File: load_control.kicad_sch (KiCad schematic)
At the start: 17 parts, among them Q20 BSB280N15NZ3, Q21 Q_NMOS_DGS, Q22 Q_NMOS_DGS, Q23 Q_NMOS_DGS, U20 LM358

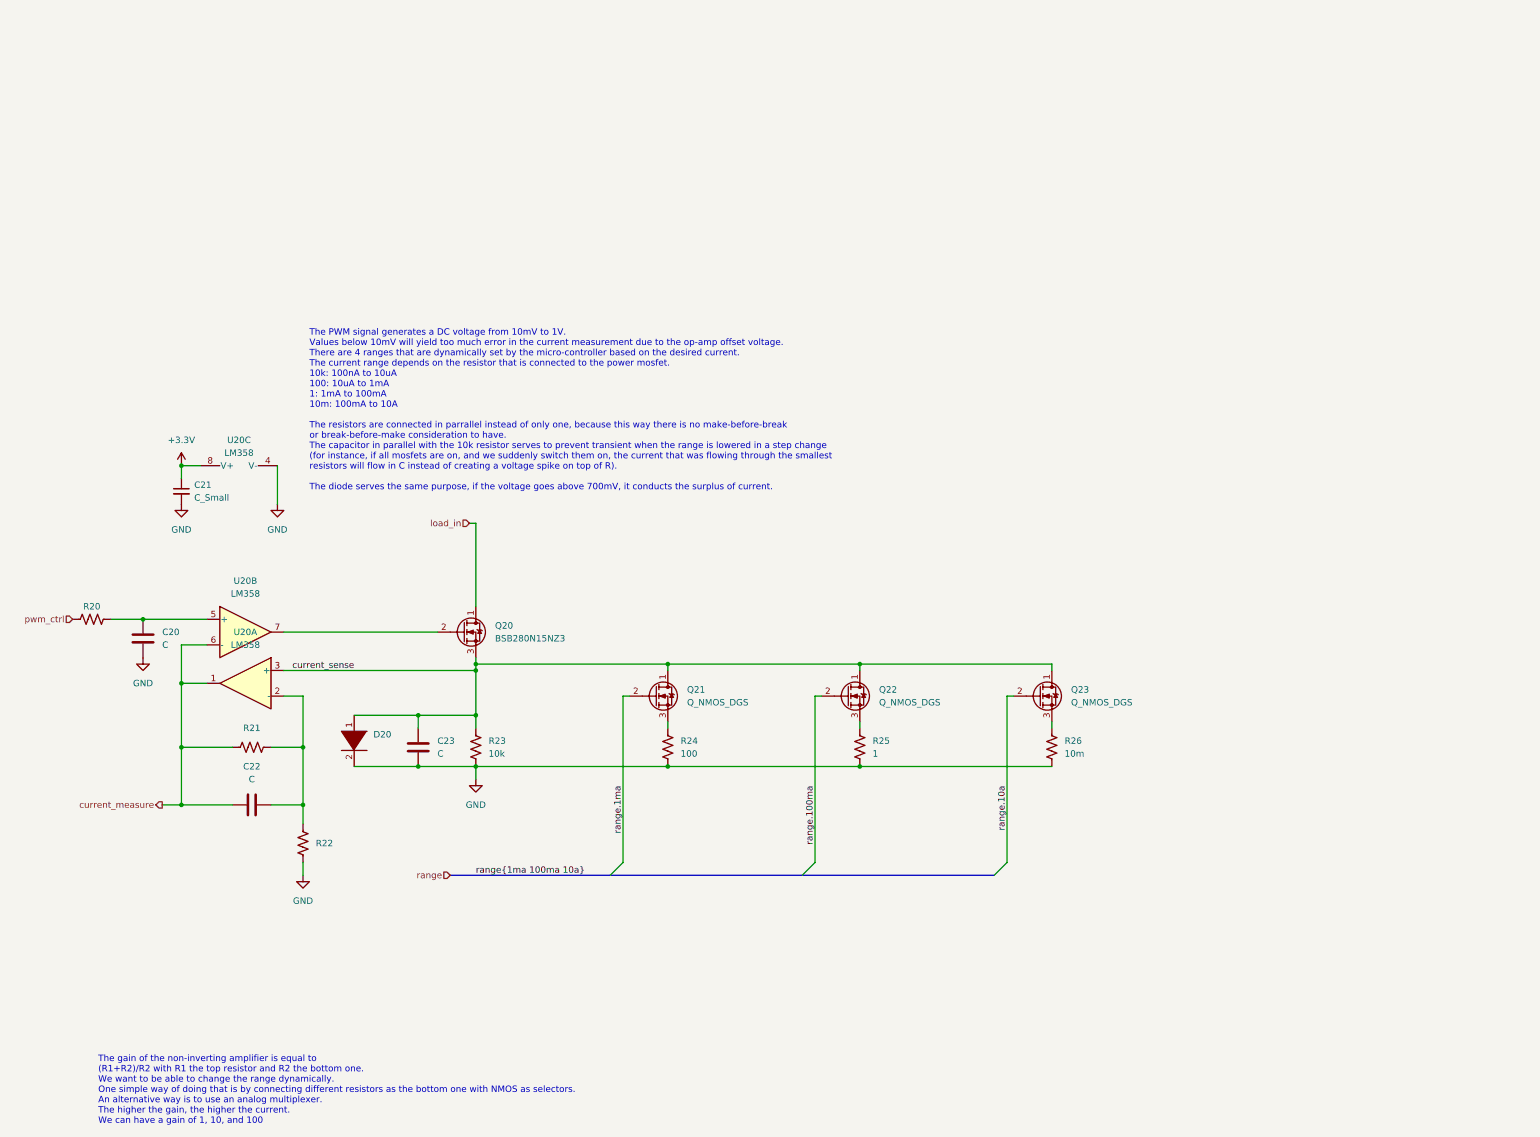
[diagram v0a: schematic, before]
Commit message: WIP PCB Routing + Add load voltage measure
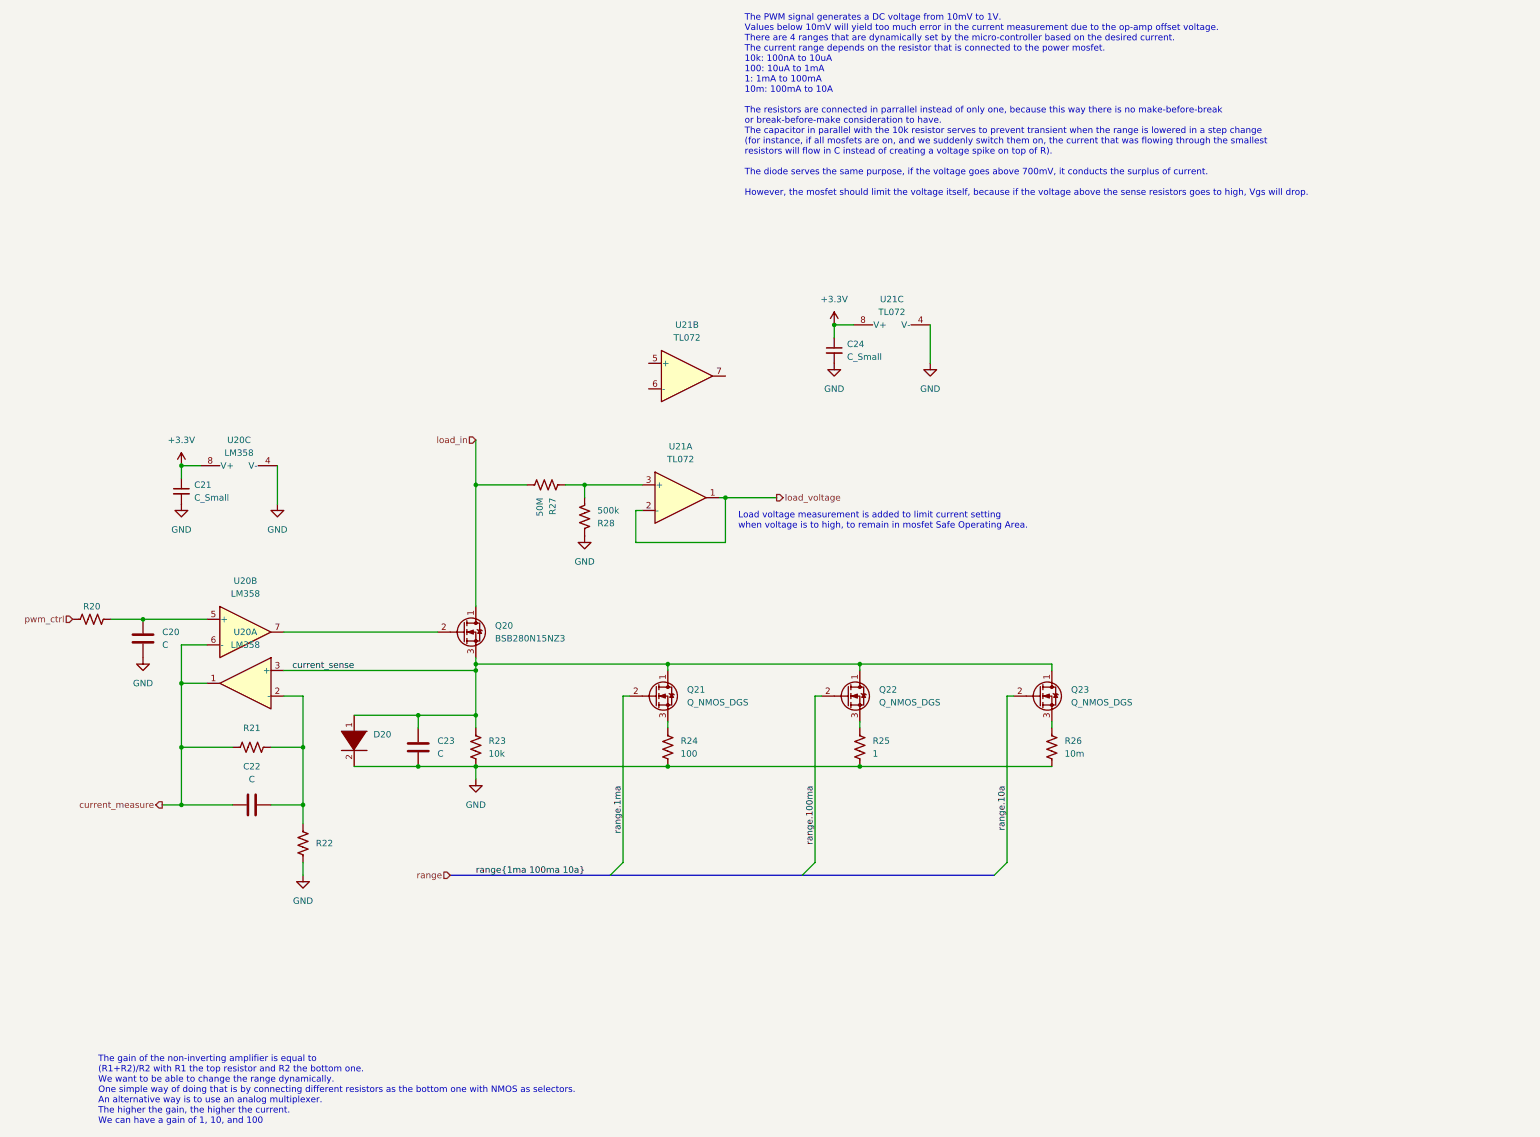
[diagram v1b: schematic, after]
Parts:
- added C24: C_Small, Capacitor_SMD:C_0805_2012Metric, symbol Device:C_Small
- added R27: 50M, Resistor_SMD:R_0805_2012Metric, symbol Device:R_US
- added R28: 500k, Resistor_SMD:R_0805_2012Metric, symbol Device:R_US
- added U21: TL072, symbol Amplifier_Operational:TL072
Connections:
- net +3V3: now also C24.1, U21.8 (V+)
- net GND: now also C24.2, R28.2, U21.4 (V-)
- net load_in: now also R27.1
- new net: R27.2, R28.1, U21.3 (+)
- new net load_voltage: U21.1, U21.2 (-)
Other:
- note added: "Load voltage measurement is added to limit current setting when voltage is to high, to remain in mosfet Safe Operating Area."

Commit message: WIP PCB Routing
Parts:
- removed Q20: BSB280N15NZ3, Package_DirectFET:DirectFET_MZ, symbol Transistor_FET:BSB280N15NZ3
- removed U21: TL072, symbol Amplifier_Operational:TL072
- added HS20: (no value), symbol Mechanical:Heatsink
- added Q20: (no value), symbol Device:Q_NMOS_GDS
- added R29: (no value), symbol Device:R_US
- added U21: (no value), symbol Amplifier_Operational:LM358
- C20, C22, C23: value C -> (none); footprint Capacitor_SMD:C_0805_2012Metric -> (none)
- C21, C24: value C_Small -> (none); footprint Capacitor_SMD:C_0805_2012Metric -> (none)
- D20: value DIODE -> (none); footprint Diode_SMD:D_0805_2012Metric -> (none)
- Q21, Q22, Q23: value Q_NMOS_DGS -> (none); footprint Package_TO_SOT_SMD:SOT-23 -> (none)
- R20, R21, R22: value R_US -> (none); footprint Resistor_SMD:R_0805_2012Metric -> (none)
- R23: value 10k -> (none); footprint Resistor_SMD:R_0805_2012Metric -> (none)
- R24: value 100 -> (none); footprint Resistor_SMD:R_0805_2012Metric -> (none)
- R25: value 1 -> (none); footprint Resistor_SMD:R_0805_2012Metric -> (none)
- R26: value 10m -> (none); footprint Resistor_SMD:R_0805_2012Metric -> (none)
- R27: value 50M -> (none); footprint Resistor_SMD:R_0805_2012Metric -> (none)
- R28: value 500k -> (none); footprint Resistor_SMD:R_0805_2012Metric -> (none)
- U20: value LM358 -> (none); footprint Package_SO:VSSOP-8_3.0x3.0mm_P0.65mm -> (none)
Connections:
- net +3V3: now also U21.8 (V+)
- net GND: now also R29.1, U21.4 (V-)
- net current_sense: now also Q20.3 (S)
- net load_in: now also Q20.2 (D)
- net load_voltage: now also U21.1, U21.2 (-)
- net at U20.7: now also Q20.1 (G), R29.2
- net at R27.2, R28.1: now also U21.3 (+)
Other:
- note added: "Load voltage measurement is added to limit current setting when voltage is too high, to remain in mosfet Safe Operating Area."
- note removed: "Load voltage measurement is added to limit current setting when voltage is to high, to remain in mosfet Safe Operating Area."
- moved on the sheet: C22, R21, R22, U20A

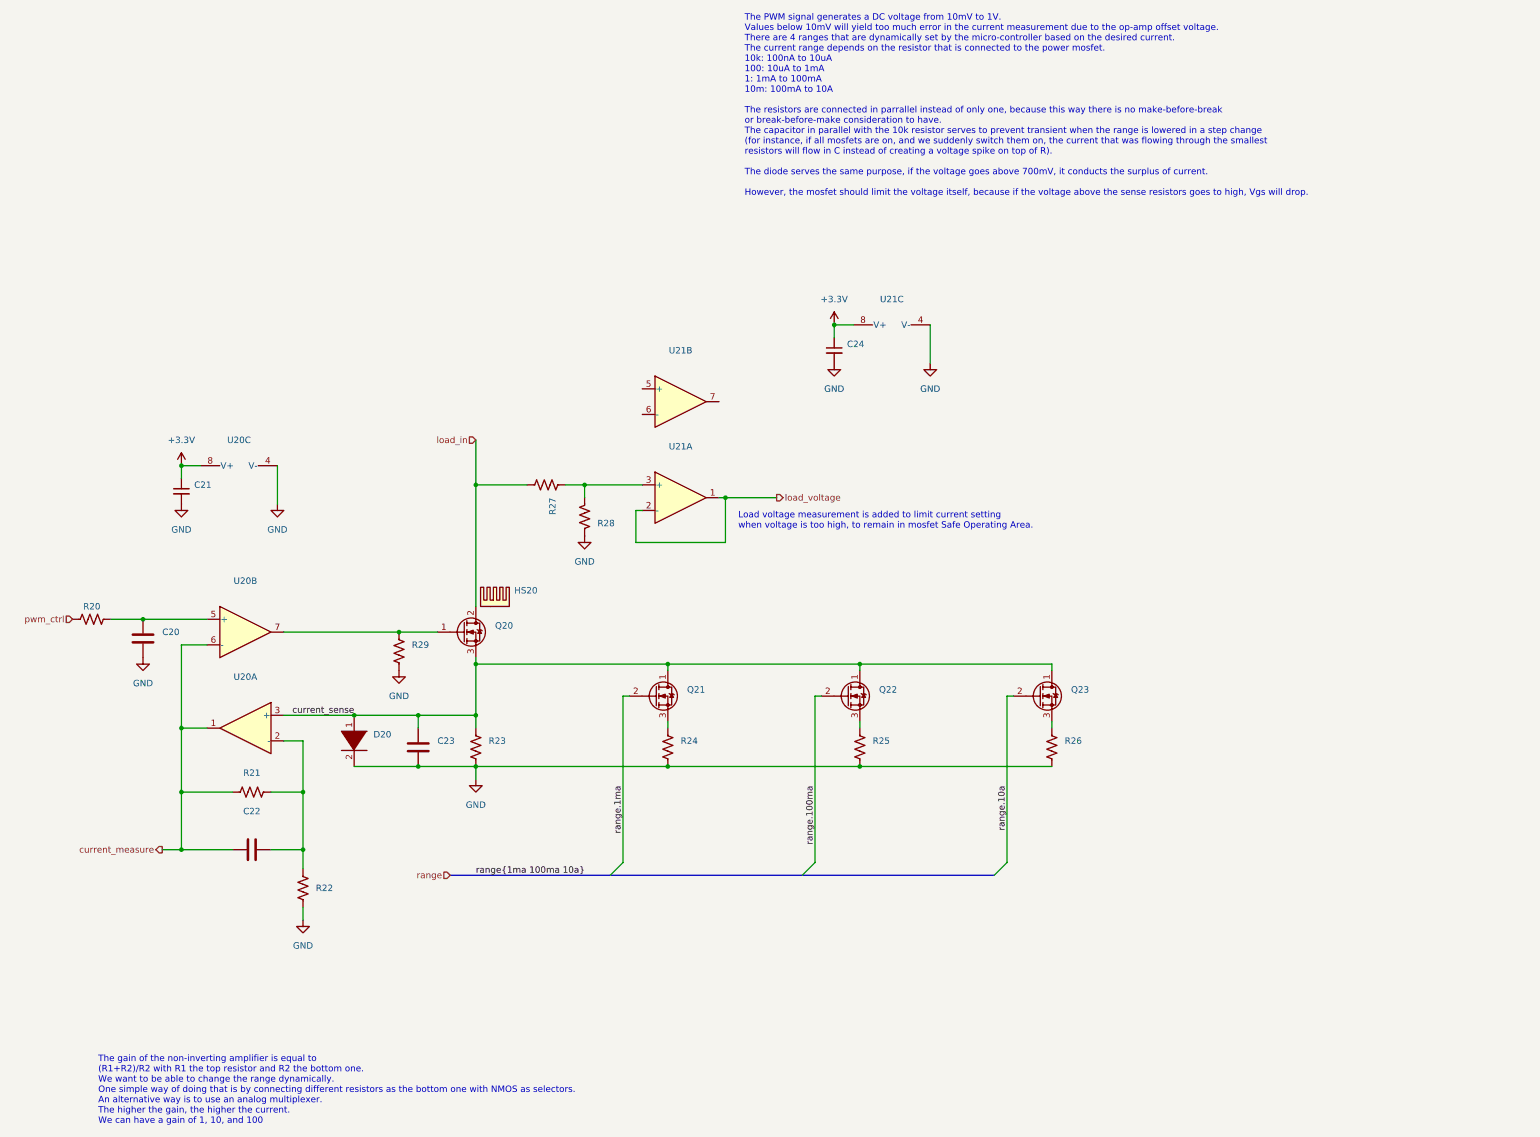
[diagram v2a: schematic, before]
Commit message: Add heatsink, among other things
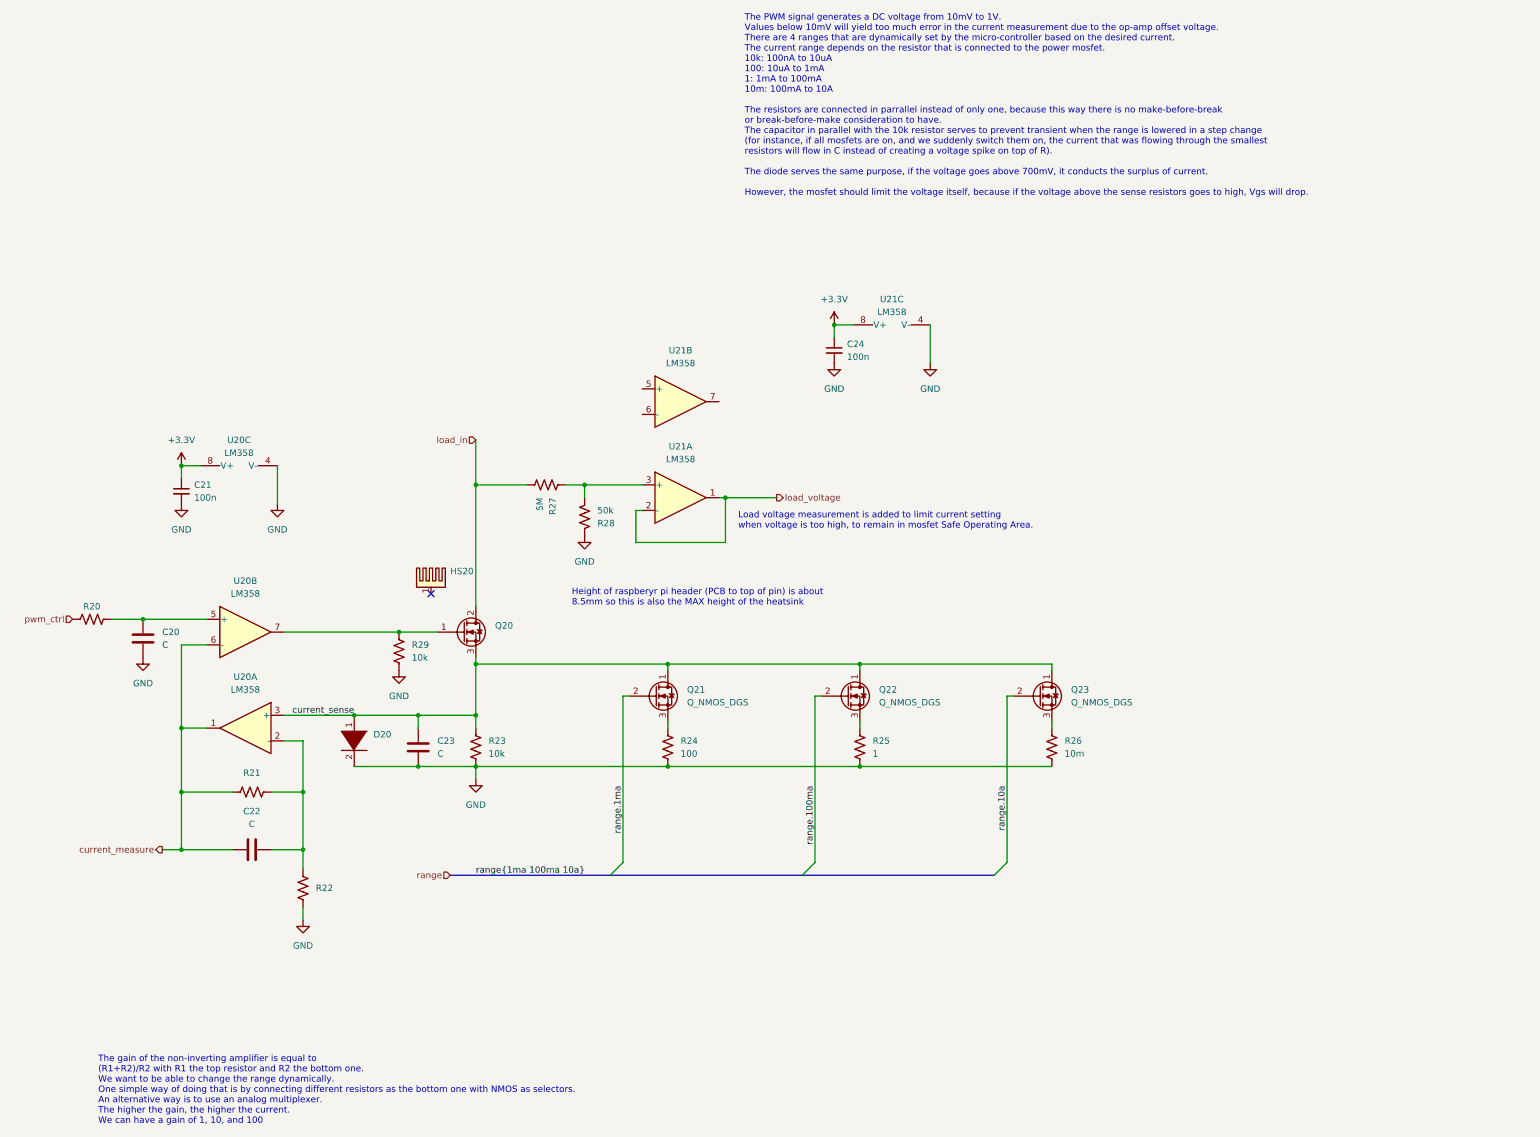
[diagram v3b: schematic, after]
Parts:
- removed HS20: (no value), symbol Mechanical:Heatsink
- added HS20: (no value), symbol Mechanical:Heatsink_Pad
- C20, C22, C23: value (none) -> C; footprint (none) -> Capacitor_SMD:C_0805_2012Metric
- C21, C24: value (none) -> 100n; footprint (none) -> Capacitor_SMD:C_0402_1005Metric
- D20: value (none) -> DIODE; footprint (none) -> Diode_SMD:D_0805_2012Metric
- Q21, Q22, Q23: value (none) -> Q_NMOS_DGS; footprint (none) -> Package_TO_SOT_SMD:SOT-23
- R20, R21, R22: value (none) -> R_US; footprint (none) -> Resistor_SMD:R_0805_2012Metric
- R23, R29: value (none) -> 10k; footprint (none) -> Resistor_SMD:R_0805_2012Metric
- R24: value (none) -> 100; footprint (none) -> Resistor_SMD:R_0805_2012Metric
- R25: value (none) -> 1; footprint (none) -> Resistor_SMD:R_0805_2012Metric
- R26: value (none) -> 10m; footprint (none) -> Resistor_SMD:R_0805_2012Metric
- R27: value (none) -> 5M; footprint (none) -> Resistor_SMD:R_0805_2012Metric
- R28: value (none) -> 50k; footprint (none) -> Resistor_SMD:R_0805_2012Metric
- U20, U21: value (none) -> LM358; footprint (none) -> Package_SO:VSSOP-8_3.0x3.0mm_P0.65mm
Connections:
- no-connect marks 0 -> 1
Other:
- note added: "Height of raspberyr pi header (PCB to top of pin) is about 8.5mm so this is also the MAX height of the heatsink"

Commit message: WIP routing
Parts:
- added R508: (no value), symbol Device:R_US
- added TH501: (no value), symbol Device:Thermistor_NTC
- C501: renamed from C20; value C -> (none); footprint Capacitor_SMD:C_0805_2012Metric -> (none)
- C502: renamed from C21; value 100n -> (none); footprint Capacitor_SMD:C_0402_1005Metric -> (none)
- C503: renamed from C22; value C -> (none); footprint Capacitor_SMD:C_0805_2012Metric -> (none)
- C504: renamed from C23; value C -> (none); footprint Capacitor_SMD:C_0805_2012Metric -> (none)
- C505: renamed from C24; value 100n -> (none); footprint Capacitor_SMD:C_0402_1005Metric -> (none)
- D501: renamed from D20; value DIODE -> (none); footprint Diode_SMD:D_0805_2012Metric -> (none)
- Q502: renamed from Q21; value Q_NMOS_DGS -> (none); footprint Package_TO_SOT_SMD:SOT-23 -> (none); symbol Device:Q_NMOS_DGS -> Device:Q_NMOS_GSD; Manufacturer (none) -> Panjit; PartNumber (none) -> PJA3404_R1_00001
- Q503: renamed from Q22; value Q_NMOS_DGS -> (none); footprint Package_TO_SOT_SMD:SOT-23 -> (none); symbol Device:Q_NMOS_DGS -> Device:Q_NMOS_GSD; Manufacturer (none) -> Panjit; PartNumber (none) -> PJA3404_R1_00001
- Q504: renamed from Q23; value Q_NMOS_DGS -> (none); footprint Package_TO_SOT_SMD:SOT-23 -> (none); symbol Device:Q_NMOS_DGS -> Device:Q_NMOS_GSD; Manufacturer (none) -> Panjit; PartNumber (none) -> PJA3404_R1_00001
- R501: renamed from R20; value R_US -> (none); footprint Resistor_SMD:R_0805_2012Metric -> (none)
- R502: renamed from R21; value R_US -> (none); footprint Resistor_SMD:R_0805_2012Metric -> (none)
- R503: renamed from R22; value R_US -> (none); footprint Resistor_SMD:R_0805_2012Metric -> (none)
- R504: renamed from R29; value 10k -> (none); footprint Resistor_SMD:R_0805_2012Metric -> (none)
- R505: renamed from R23; value 10k -> (none); footprint Resistor_SMD:R_0805_2012Metric -> (none)
- R506: renamed from R27; value 5M -> (none); footprint Resistor_SMD:R_0805_2012Metric -> (none)
- R507: renamed from R28; value 50k -> (none); footprint Resistor_SMD:R_0805_2012Metric -> (none)
- R509: renamed from R24; value 100 -> (none); footprint Resistor_SMD:R_0805_2012Metric -> (none)
- R510: renamed from R25; value 1 -> (none); footprint Resistor_SMD:R_0805_2012Metric -> (none)
- R511: renamed from R26; value 10m -> (none); footprint Resistor_SMD:R_0805_2012Metric -> (none)
- U501: renamed from U20; value LM358 -> (none); footprint Package_SO:VSSOP-8_3.0x3.0mm_P0.65mm -> (none)
- U502: renamed from U21; value LM358 -> (none); footprint Package_SO:VSSOP-8_3.0x3.0mm_P0.65mm -> (none)
- renumbered HS20 to HS501, Q20 to Q501
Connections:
- net +3V3: no longer C502.1, U501.8 (V+)
- net GND: now also TH501.2
- net current_sense: now also Q502.3 (D), Q503.3 (D), Q504.3 (D); no longer Q502.1 (D), Q503.1 (D), Q504.1 (D)
- net range.100ma: now also Q503.1 (G); no longer Q503.2 (G)
- net range.10a: now also Q504.1 (G); no longer Q504.2 (G)
- net range.1ma: now also Q502.1 (G); no longer Q502.2 (G)
- net at R509.2: now also Q502.2 (S); no longer Q502.3 (S)
- net at R511.2: now also Q504.2 (S); no longer Q504.3 (S)
- net at R510.2: now also Q503.2 (S); no longer Q503.3 (S)
- net at U502.5 (+): now also R508.2, TH501.1
- net temp_sense: now reaches U502.6 (-)
- net temp_sense: now also U502.7
- new net +5V: C502.1, U501.8 (V+)
- new net temp_en: R508.1
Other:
- note removed: "Height of raspberyr pi header (PCB to top of pin) is about 8.5mm so this is also the MAX height of the heatsink"
- moved on the sheet: R506, R507, U502A, U502B
